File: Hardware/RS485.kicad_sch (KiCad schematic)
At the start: 18 parts, among them J5 Conn_01x02_Male, J6 Screw_Terminal_01x02, U9 SP3485EN

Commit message: add shematics MVA
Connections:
- net at F2.2: now also J6.1 (Pin_1); no longer J6.2 (Pin_2)
- net at F1.2: now also J6.2 (Pin_2); no longer J6.1 (Pin_1)
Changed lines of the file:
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@@
     )
   )
-  (symbol (lib_id "Connector:Screw_Terminal_01x02") (at 208.28 78.74 0) (unit 1)
-    (in_bom yes) (on_board yes) (dnp no) (fields_autoplaced)
-    (property "Reference" "J6" (at 210.82 78.7399 0)
+  (symbol (lib_id "Connector:Screw_Terminal_01x02") (at 208.28 81.28 0) (mirror x) (unit 1)
+    (in_bom yes) (on_board yes) (dnp no)
+    (property "Reference" "J6" (at 210.82 81.2801 0)
       (effects (font (size 1.27 1.27)) (justify left))
     )
-    (property "Value" "Screw_Terminal_01x02" (at 210.82 81.2799 0)
+    (property "Value" "Screw_Terminal_01x02" (at 210.82 78.7401 0)
       (effects (font (size 1.27 1.27)) (justify left) hide)
     )
-    (property "Footprint" "IVS_FOOTPRINTS:HT-3.96mm-2Pin" (at 208.28 78.74 0)
+    (property "Footprint" "IVS_FOOTPRINTS:HT-3.96mm-2Pin" (at 208.28 81.28 0)
       (effects (font (size 1.27 1.27)) hide)
     )
-    (property "Datasheet" "~" (at 208.28 78.74 0)
+    (property "Datasheet" "~" (at 208.28 81.28 0)
       (effects (font (size 1.27 1.27)) hide)
     )

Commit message: layout PCB part 1
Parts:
- removed J6: Screw_Terminal_01x02, IVS_FOOTPRINTS:HT-3.96mm-2Pin, symbol Connector:Screw_Terminal_01x02
- added J11: Screw_Terminal, IVS_FOOTPRINTS:Terminal_HT-P3.96mm-3P-Vertical-Pluggable, symbol Connector:Screw_Terminal_01x03
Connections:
- net Earth: now also J11.1 (Pin_1); no longer D5.1
- net GND: now also D5.1
- net B2_RS485: now reaches R26.2, R28.1, U9.7 (B)
- net B1_RS485: now reaches D6.2, D7.1, F2.1, J5.1 (Pin_1), R28.2
- net A2_RS485: now reaches R25.1, R27.1, U9.6 (A)
- net A1_RS485: now reaches D5.2, D6.1, F1.1, R27.2, R29.1
- net B_RS485: now reaches F2.2
- net B_RS485: now also J11.2 (Pin_2)
- net A_RS485: now reaches F1.2
- net A_RS485: now also J11.3 (Pin_3)
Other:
- moved on the sheet: D5
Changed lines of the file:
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@@
   (junction (at 167.64 74.93) (diameter 0) (color 0 0 0 0)
   )
+  (junction (at 167.64 109.22) (diameter 0) (color 0 0 0 0)
+  )
   (junction (at 160.02 109.22) (diameter 0) (color 0 0 0 0)
   )
@@
   (junction (at 167.64 99.06) (diameter 0) (color 0 0 0 0)
   )
+  (junction (at 158.75 99.06) (diameter 0) (color 0 0 0 0)
+  )
   (junction (at 109.22 99.06) (diameter 0) (color 0 0 0 0)
   )
@@
   (junction (at 152.4 74.93) (diameter 0) (color 0 0 0 0)
   )
+  (junction (at 158.75 74.93) (diameter 0) (color 0 0 0 0)
+  )
   (junction (at 130.81 85.09) (diameter 0) (color 0 0 0 0)
   )
@@
     (stroke (width 0) (type default))
   )
-  (wire (pts (xy 167.64 73.66) (xy 167.64 74.93))
-    (stroke (width 0) (type default))
-  )
   (wire (pts (xy 152.4 72.39) (xy 152.4 74.93))
     (stroke (width 0) (type default))
@@
     (stroke (width 0) (type default))
   )
-  (wire (pts (xy 152.4 74.93) (xy 167.64 74.93))
+  (wire (pts (xy 152.4 74.93) (xy 158.75 74.93))
     (stroke (width 0) (type default))
   )
@@
     (stroke (width 0) (type default))
   )
+  (wire (pts (xy 203.2 83.82) (xy 203.2 109.22))
+    (stroke (width 0) (type default))
+  )
+  (wire (pts (xy 158.75 74.93) (xy 167.64 74.93))
+    (stroke (width 0) (type default))
+  )
   (wire (pts (xy 130.81 85.09) (xy 135.89 85.09))
     (stroke (width 0) (type default))
@@
     (stroke (width 0) (type default))
   )
+  (wire (pts (xy 158.75 96.52) (xy 158.75 99.06))
+    (stroke (width 0) (type default))
+  )
   (wire (pts (xy 167.64 107.95) (xy 167.64 109.22))
     (stroke (width 0) (type default))
@@
     (stroke (width 0) (type default))
   )
-  (wire (pts (xy 167.64 62.23) (xy 167.64 63.5))
-    (stroke (width 0) (type default))
-  )
   (wire (pts (xy 76.2 80.01) (xy 99.06 80.01))
     (stroke (width 0) (type default))
@@
     (stroke (width 0) (type default))
   )
+  (wire (pts (xy 158.75 99.06) (xy 167.64 99.06))
+    (stroke (width 0) (type default))
+  )
   (wire (pts (xy 167.64 99.06) (xy 167.64 100.33))
     (stroke (width 0) (type default))
   )
+  (wire (pts (xy 158.75 74.93) (xy 158.75 86.36))
+    (stroke (width 0) (type default))
+  )
   (wire (pts (xy 109.22 106.68) (xy 109.22 99.06))
     (stroke (width 0) (type default))
@@
     (stroke (width 0) (type default))
   )
-  (wire (pts (xy 152.4 99.06) (xy 167.64 99.06))
+  (wire (pts (xy 152.4 99.06) (xy 158.75 99.06))
     (stroke (width 0) (type default))
   )
   (polyline (pts (xy 236.22 151.13) (xy 236.22 39.37))
+    (stroke (width 0) (type default))
+  )
+  (wire (pts (xy 203.2 109.22) (xy 167.64 109.22))
     (stroke (width 0) (type default))
   )
@@
     (effects (font (size 5 5) bold) (justify left bottom))
   )
+  (label "B2_RS485" (at 128.905 85.09 180) (fields_autoplaced)
+    (effects (font (size 1.27 1.27)) (justify right bottom))
+  )
+  (label "B_RS485" (at 192.405 85.09 0) (fields_autoplaced)
+    (effects (font (size 1.27 1.27)) (justify left bottom))
+  )
   (label "RS485.RX" (at 87.63 101.6 180) (fields_autoplaced)
     (effects (font (size 1.27 1.27)) (justify right bottom))
   )
+  (label "A_RS485" (at 191.77 74.93 0) (fields_autoplaced)
+    (effects (font (size 1.27 1.27)) (justify left bottom))
+  )
   (label "RS485.TX" (at 76.2 85.09 180) (fields_autoplaced)
     (effects (font (size 1.27 1.27)) (justify right bottom))
@@
   )
   (label "RS485.TX" (at 87.63 96.52 180) (fields_autoplaced)
+    (effects (font (size 1.27 1.27)) (justify right bottom))
+  )
+  (label "A1_RS485" (at 152.4 74.93 180) (fields_autoplaced)
+    (effects (font (size 1.27 1.27)) (justify right bottom))
+  )
+  (label "B1_RS485" (at 152.4 85.09 180) (fields_autoplaced)
+    (effects (font (size 1.27 1.27)) (justify right bottom))
+  )
+  (label "A2_RS485" (at 128.905 74.93 180) (fields_autoplaced)
     (effects (font (size 1.27 1.27)) (justify right bottom))
   )
@@
     )
   )
+  (symbol (lib_id "Connector:Screw_Terminal_01x03") (at 208.28 81.28 0) (mirror x) (unit 1)
+    (in_bom yes) (on_board yes) (dnp no)
+    (property "Reference" "J11" (at 211.455 81.2801 0)
+      (effects (font (size 1.27 1.27)) (justify left))
+    )
+    (property "Value" "Screw_Terminal" (at 210.82 80.0101 0)
+      (effects (font (size 1.27 1.27)) (justify left) hide)
+    )
+    (property "Footprint" "IVS_FOOTPRINTS:Terminal_HT-P3.96mm-3P-Vertical-Pluggable" (at 208.28 81.28 0)
+      (effects (font (size 1.27 1.27)) hide)
+    )
+    (property "Datasheet" "~" (at 208.28 81.28 0)
+      (effects (font (size 1.27 1.27)) hide)
+    )
+    (pin "1")
+    (pin "2")
+    (pin "3")
+    (instances
+      (project "dongtam"
+        (path "/6833aec4-3d1d-4261-9b3e-f0452b565dd3/20e0764d-b27c-4f4c-b032-197976a30834"
+          (reference "J11") (unit 1)
+        )
+        (path "/6833aec4-3d1d-4261-9b3e-f0452b565dd3/1f85aaf5-5de5-40f1-af11-1d1001353a81"
+          (reference "J14") (unit 1)
+        )
+      )
+    )
+  )
   (symbol (lib_id "Connector:Conn_01x02_Male") (at 154.94 57.15 270) (unit 1)
     (in_bom yes) (on_board yes) (dnp no)
@@
     )
   )
-  (symbol (lib_id "power:Earth") (at 167.64 62.23 180) (unit 1)
-    (in_bom yes) (on_board yes) (dnp no) (fields_autoplaced)
-    (property "Reference" "#PWR066" (at 167.64 55.88 0)
-      (effects (font (size 1.27 1.27)) hide)
-    )
-    (property "Value" "Earth" (at 167.64 58.42 0)
-      (effects (font (size 1.27 1.27)) hide)
-    )
-    (property "Footprint" "" (at 167.64 62.23 0)
-      (effects (font (size 1.27 1.27)) hide)
-    )
-    (property "Datasheet" "~" (at 167.64 62.23 0)
-      (effects (font (size 1.27 1.27)) hide)
-    )
-    (pin "1")
-    (instances
-      (project "dongtam"
-        (path "/6833aec4-3d1d-4261-9b3e-f0452b565dd3/1f85aaf5-5de5-40f1-af11-1d1001353a81"
-          (reference "#PWR066") (unit 1)
-        )
-      )
-    )
-  )
   (symbol (lib_id "Device:Polyfuse") (at 185.42 85.09 90) (unit 1)
     (in_bom yes) (on_board yes) (dnp no)
@@
     )
   )
-  (symbol (lib_id "Connector:Screw_Terminal_01x02") (at 208.28 81.28 0) (mirror x) (unit 1)
-    (in_bom yes) (on_board yes) (dnp no)
-    (property "Reference" "J6" (at 210.82 81.2801 0)
-      (effects (font (size 1.27 1.27)) (justify left))
-    )
-    (property "Value" "Screw_Terminal_01x02" (at 210.82 78.7401 0)
-      (effects (font (size 1.27 1.27)) (justify left) hide)
-    )
-    (property "Footprint" "IVS_FOOTPRINTS:HT-3.96mm-2Pin" (at 208.28 81.28 0)
-      (effects (font (size 1.27 1.27)) hide)
-    )
-    (property "Datasheet" "~" (at 208.28 81.28 0)
-      (effects (font (size 1.27 1.27)) hide)
-    )
-    (pin "1")
-    (pin "2")
-    (instances
-      (project "dongtam"
-        (path "/6833aec4-3d1d-4261-9b3e-f0452b565dd3/1f85aaf5-5de5-40f1-af11-1d1001353a81"
-          (reference "J6") (unit 1)
-        )
-      )
-    )
-  )
   (symbol (lib_id "Device:Polyfuse") (at 185.42 74.93 90) (unit 1)
     (in_bom yes) (on_board yes) (dnp no) (fields_autoplaced)
@@
     )
   )
-  (symbol (lib_id "IVS_SYMBOL_DIR:D_TVS") (at 167.64 68.58 90) (unit 1)
-    (in_bom yes) (on_board yes) (dnp no) (fields_autoplaced)
-    (property "Reference" "D5" (at 170.18 67.3099 90)
-      (effects (font (size 1.27 1.27)) (justify right))
-    )
-    (property "Value" "D_TVS" (at 170.18 69.8499 90)
-      (effects (font (size 1.27 1.27)) (justify right))
-    )
-    (property "Footprint" "IVS_FOOTPRINTS:D_SMA" (at 167.64 68.58 0)
-      (effects (font (size 1.27 1.27)) hide)
-    )
-    (property "Datasheet" "" (at 167.64 68.58 0)
-      (effects (font (size 1.27 1.27)) hide)
-    )
+  (symbol (lib_id "IVS_SYMBOL_DIR:D_TVS") (at 158.75 91.44 270) (unit 1)
+    (in_bom yes) (on_board yes) (dnp no)
+    (property "Reference" "D5" (at 150.495 90.805 90)
+      (effects (font (size 1.27 1.27)) (justify left))
+    )
+    (property "Value" "D_TVS" (at 150.495 93.345 90)
+      (effects (font (size 1.27 1.27)) (justify left))
+    )
+    (property "Footprint" "IVS_FOOTPRINTS:D_SMA" (at 158.75 91.44 0)
+      (effects (font (size 1.27 1.27)) hide)
+    )
+    (property "Datasheet" "" (at 158.75 91.44 0)
+      (effects (font (size 1.27 1.27)) hide)
+    )

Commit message: layout part 2
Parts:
- removed J11: Screw_Terminal, IVS_FOOTPRINTS:Terminal_HT-P3.96mm-3P-Vertical-Pluggable, symbol Connector:Screw_Terminal_01x03
- added J15: Conn_01x05_Pin, IVS_FOOTPRINTS:Terminal_HT-3.96mm-5P-Vertical-Pluggable, symbol Connector:Conn_01x05_Pin
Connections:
- net A_RS485: now also J15.3 (Pin_3), J15.5 (Pin_5)
- net B_RS485: now also J15.2 (Pin_2), J15.4 (Pin_4)
- net Earth: now also J15.1 (Pin_1)
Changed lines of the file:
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@@
   (junction (at 125.73 99.06) (diameter 0) (color 0 0 0 0)
   )
+  (junction (at 203.835 78.74) (diameter 0) (color 0 0 0 0)
+  )
   (junction (at 99.06 80.01) (diameter 0) (color 0 0 0 0)
   )
@@
   (junction (at 109.22 99.06) (diameter 0) (color 0 0 0 0)
   )
+  (junction (at 205.105 81.28) (diameter 0) (color 0 0 0 0)
+  )
   (junction (at 154.94 85.09) (diameter 0) (color 0 0 0 0)
   )
@@
     (stroke (width 0) (type default))
   )
-  (wire (pts (xy 201.93 81.28) (xy 203.2 81.28))
+  (wire (pts (xy 201.93 81.28) (xy 205.105 81.28))
     (stroke (width 0) (type default))
   )
@@
     (stroke (width 0) (type default))
   )
+  (wire (pts (xy 203.2 83.82) (xy 206.375 83.82))
+    (stroke (width 0) (type default))
+  )
   (wire (pts (xy 167.64 74.93) (xy 181.61 74.93))
     (stroke (width 0) (type default))
   )
+  (wire (pts (xy 205.105 81.28) (xy 206.375 81.28))
+    (stroke (width 0) (type default))
+  )
   (wire (pts (xy 201.93 74.93) (xy 201.93 78.74))
     (stroke (width 0) (type default))
@@
     (stroke (width 0) (type default))
   )
+  (wire (pts (xy 206.375 73.66) (xy 203.835 73.66))
+    (stroke (width 0) (type default))
+  )
   (wire (pts (xy 96.52 63.5) (xy 99.06 63.5))
     (stroke (width 0) (type default))
@@
     (stroke (width 0) (type default))
   )
+  (wire (pts (xy 206.375 76.2) (xy 205.105 76.2))
+    (stroke (width 0) (type default))
+  )
   (wire (pts (xy 119.38 82.55) (xy 119.38 85.09))
     (stroke (width 0) (type default))
   )
+  (wire (pts (xy 205.105 76.2) (xy 205.105 81.28))
+    (stroke (width 0) (type default))
+  )
   (wire (pts (xy 152.4 99.06) (xy 152.4 100.33))
     (stroke (width 0) (type default))
@@
     (stroke (width 0) (type default))
   )
-  (wire (pts (xy 201.93 78.74) (xy 203.2 78.74))
+  (wire (pts (xy 201.93 78.74) (xy 203.835 78.74))
     (stroke (width 0) (type default))
   )
@@
     (stroke (width 0) (type default))
   )
+  (wire (pts (xy 203.835 78.74) (xy 206.375 78.74))
+    (stroke (width 0) (type default))
+  )
   (wire (pts (xy 158.75 96.52) (xy 158.75 99.06))
     (stroke (width 0) (type default))
@@
   )
   (wire (pts (xy 109.22 106.68) (xy 109.22 99.06))
+    (stroke (width 0) (type default))
+  )
+  (wire (pts (xy 203.835 73.66) (xy 203.835 78.74))
     (stroke (width 0) (type default))
   )
@@
     )
   )
-  (symbol (lib_id "Connector:Screw_Terminal_01x03") (at 208.28 81.28 0) (mirror x) (unit 1)
-    (in_bom yes) (on_board yes) (dnp no)
-    (property "Reference" "J11" (at 211.455 81.2801 0)
-      (effects (font (size 1.27 1.27)) (justify left))
-    )
-    (property "Value" "Screw_Terminal" (at 210.82 80.0101 0)
-      (effects (font (size 1.27 1.27)) (justify left) hide)
-    )
-    (property "Footprint" "IVS_FOOTPRINTS:Terminal_HT-P3.96mm-3P-Vertical-Pluggable" (at 208.28 81.28 0)
-      (effects (font (size 1.27 1.27)) hide)
-    )
-    (property "Datasheet" "~" (at 208.28 81.28 0)
-      (effects (font (size 1.27 1.27)) hide)
-    )
-    (pin "1")
-    (pin "2")
-    (pin "3")
-    (instances
-      (project "dongtam"
-        (path "/6833aec4-3d1d-4261-9b3e-f0452b565dd3/20e0764d-b27c-4f4c-b032-197976a30834"
-          (reference "J11") (unit 1)
-        )
-        (path "/6833aec4-3d1d-4261-9b3e-f0452b565dd3/1f85aaf5-5de5-40f1-af11-1d1001353a81"
-          (reference "J14") (unit 1)
-        )
-      )
-    )
-  )
   (symbol (lib_id "Connector:Conn_01x02_Male") (at 154.94 57.15 270) (unit 1)
     (in_bom yes) (on_board yes) (dnp no)
@@
         )
       )
+    )
+  )
+  (symbol (lib_id "Connector:Conn_01x05_Pin") (at 211.455 78.74 180) (unit 1)
+    (in_bom yes) (on_board yes) (dnp no) (fields_autoplaced)
+    (property "Reference" "J15" (at 212.725 78.105 0)
+      (effects (font (size 1.27 1.27)) (justify right))
+    )
+    (property "Value" "Conn_01x05_Pin" (at 212.725 80.645 0)
+      (effects (font (size 1.27 1.27)) (justify right))
+    )
+    (property "Footprint" "IVS_FOOTPRINTS:Terminal_HT-3.96mm-5P-Vertical-Pluggable" (at 211.455 78.74 0)
+      (effects (font (size 1.27 1.27)) hide)
+    )
+    (property "Datasheet" "~" (at 211.455 78.74 0)
+      (effects (font (size 1.27 1.27)) hide)
+    )
+    (pin "1")
+    (pin "2")
+    (pin "3")
+    (pin "4")
+    (pin "5")
+    (instances
+      (project "dongtam"
+        (path "/6833aec4-3d1d-4261-9b3e-f0452b565dd3/1f85aaf5-5de5-40f1-af11-1d1001353a81"
+          (reference "J15") (unit 1)
+        )
+      )

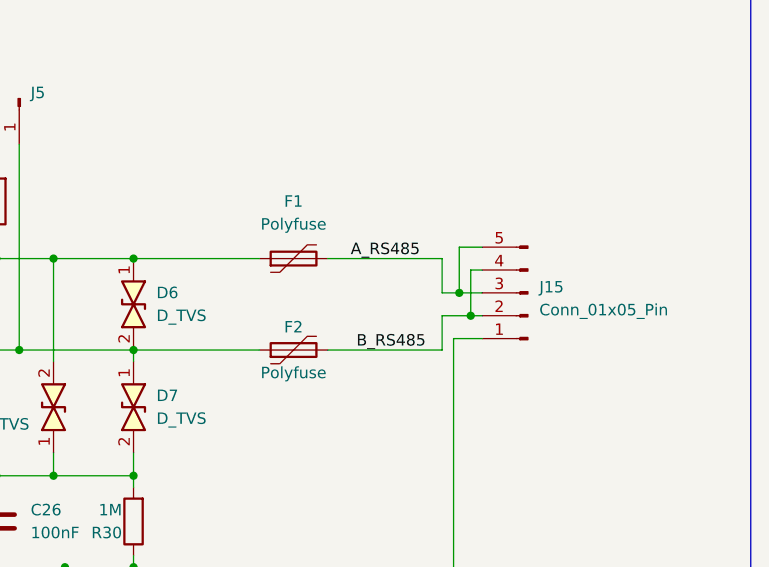
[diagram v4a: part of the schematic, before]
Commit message: add level shifter Hc595 ESP32
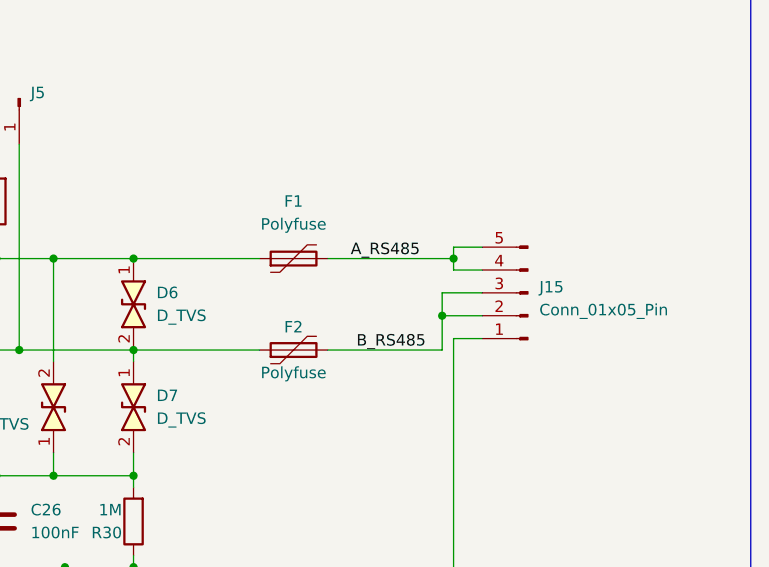
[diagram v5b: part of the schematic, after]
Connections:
- net A_RS485: now also J15.4 (Pin_4); no longer J15.3 (Pin_3)
- net B_RS485: now also J15.3 (Pin_3); no longer J15.4 (Pin_4)
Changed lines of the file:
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@@
   (junction (at 125.73 99.06) (diameter 0) (color 0 0 0 0)
   )
-  (junction (at 203.835 78.74) (diameter 0) (color 0 0 0 0)
-  )
   (junction (at 99.06 80.01) (diameter 0) (color 0 0 0 0)
   )
+  (junction (at 203.2 74.93) (diameter 0) (color 0 0 0 0)
+  )
   (junction (at 167.64 99.06) (diameter 0) (color 0 0 0 0)
   )
@@
   (junction (at 109.22 99.06) (diameter 0) (color 0 0 0 0)
   )
-  (junction (at 205.105 81.28) (diameter 0) (color 0 0 0 0)
+  (junction (at 201.93 81.28) (diameter 0) (color 0 0 0 0)
   )
   (junction (at 154.94 85.09) (diameter 0) (color 0 0 0 0)
@@
     (stroke (width 0) (type default))
   )
-  (wire (pts (xy 201.93 81.28) (xy 205.105 81.28))
+  (wire (pts (xy 201.93 81.28) (xy 206.375 81.28))
     (stroke (width 0) (type default))
   )
@@
     (stroke (width 0) (type default))
   )
-  (wire (pts (xy 205.105 81.28) (xy 206.375 81.28))
-    (stroke (width 0) (type default))
-  )
-  (wire (pts (xy 201.93 74.93) (xy 201.93 78.74))
-    (stroke (width 0) (type default))
-  )
   (wire (pts (xy 99.06 80.01) (xy 99.06 82.55))
     (stroke (width 0) (type default))
   )
+  (wire (pts (xy 203.2 74.93) (xy 203.2 76.2))
+    (stroke (width 0) (type default))
+  )
   (wire (pts (xy 97.155 74.93) (xy 99.06 74.93))
     (stroke (width 0) (type default))
@@
     (stroke (width 0) (type default))
   )
-  (wire (pts (xy 206.375 73.66) (xy 203.835 73.66))
-    (stroke (width 0) (type default))
-  )
   (wire (pts (xy 96.52 63.5) (xy 99.06 63.5))
     (stroke (width 0) (type default))
@@
     (stroke (width 0) (type default))
   )
+  (wire (pts (xy 203.2 73.66) (xy 203.2 74.93))
+    (stroke (width 0) (type default))
+  )
   (wire (pts (xy 106.68 63.5) (xy 109.22 63.5))
     (stroke (width 0) (type default))
@@
     (stroke (width 0) (type default))
   )
-  (wire (pts (xy 206.375 76.2) (xy 205.105 76.2))
-    (stroke (width 0) (type default))
-  )
   (wire (pts (xy 119.38 82.55) (xy 119.38 85.09))
     (stroke (width 0) (type default))
   )
-  (wire (pts (xy 205.105 76.2) (xy 205.105 81.28))
-    (stroke (width 0) (type default))
-  )
   (wire (pts (xy 152.4 99.06) (xy 152.4 100.33))
     (stroke (width 0) (type default))
@@
     (stroke (width 0) (type default))
   )
-  (wire (pts (xy 189.23 74.93) (xy 201.93 74.93))
+  (wire (pts (xy 189.23 74.93) (xy 203.2 74.93))
+    (stroke (width 0) (type default))
+  )
+  (wire (pts (xy 206.375 73.66) (xy 203.2 73.66))
     (stroke (width 0) (type default))
   )
@@
     (stroke (width 0) (type default))
   )
-  (wire (pts (xy 201.93 78.74) (xy 203.835 78.74))
-    (stroke (width 0) (type default))
-  )
   (wire (pts (xy 99.06 77.47) (xy 99.06 80.01))
     (stroke (width 0) (type default))
@@
     (stroke (width 0) (type default))
   )
+  (wire (pts (xy 203.2 76.2) (xy 206.375 76.2))
+    (stroke (width 0) (type default))
+  )
   (wire (pts (xy 76.2 85.09) (xy 88.9 85.09))
     (stroke (width 0) (type default))
@@
     (stroke (width 0) (type default))
   )
-  (wire (pts (xy 203.835 78.74) (xy 206.375 78.74))
-    (stroke (width 0) (type default))
-  )
   (wire (pts (xy 158.75 96.52) (xy 158.75 99.06))
     (stroke (width 0) (type default))
@@
     (stroke (width 0) (type default))
   )
+  (wire (pts (xy 201.93 78.74) (xy 201.93 81.28))
+    (stroke (width 0) (type default))
+  )
   (wire (pts (xy 167.64 99.06) (xy 167.64 100.33))
     (stroke (width 0) (type default))
@@
     (stroke (width 0) (type default))
   )
-  (wire (pts (xy 203.835 73.66) (xy 203.835 78.74))
-    (stroke (width 0) (type default))
-  )
   (wire (pts (xy 167.64 96.52) (xy 167.64 99.06))
     (stroke (width 0) (type default))
@@
     (stroke (width 0) (type default))
   )
+  (wire (pts (xy 206.375 78.74) (xy 201.93 78.74))
+    (stroke (width 0) (type default))
+  )
